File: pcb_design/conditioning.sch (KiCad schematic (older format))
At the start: 39 parts, among them U3 OPA2376AID, U4 LM2903-SO8

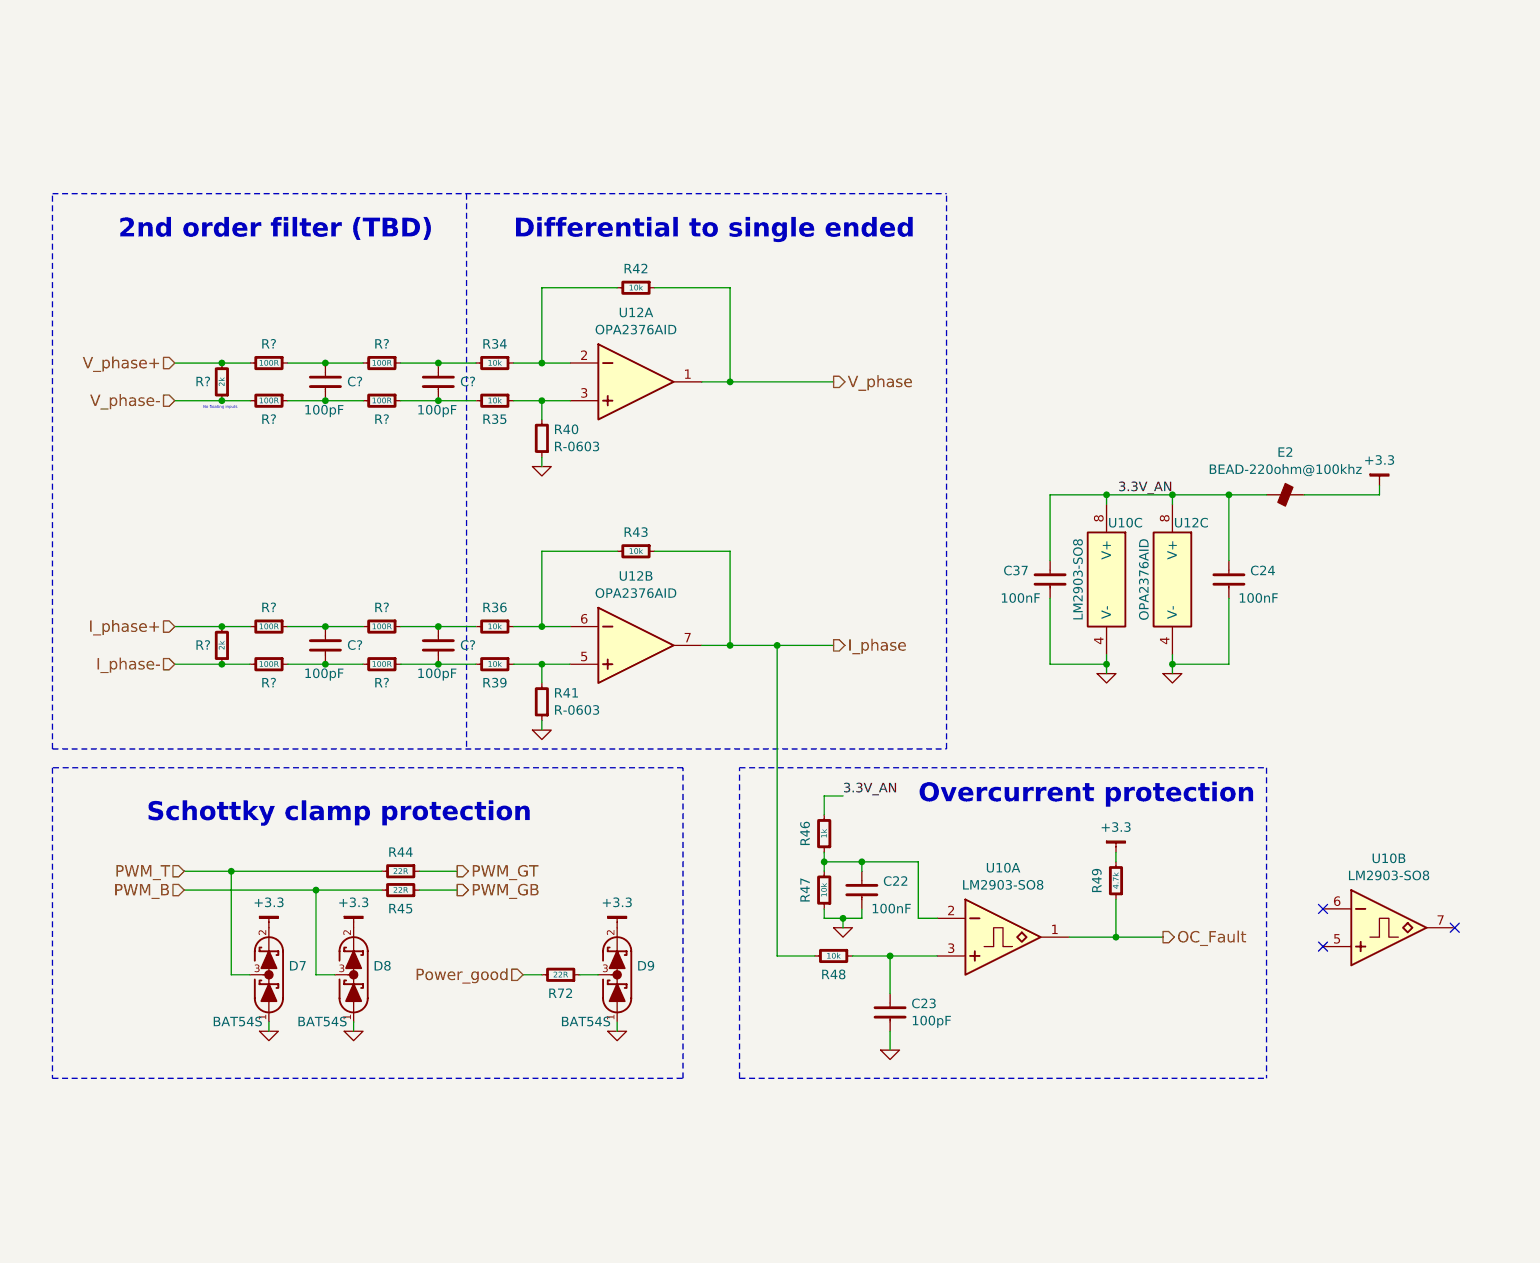
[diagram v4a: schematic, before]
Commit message: Added bus voltage conditioning, %v to accel and regen inputs, regulator diode, annotated schematic
Signed-off-by: Marcos Chaparro <mchaparro@paltatech.com>
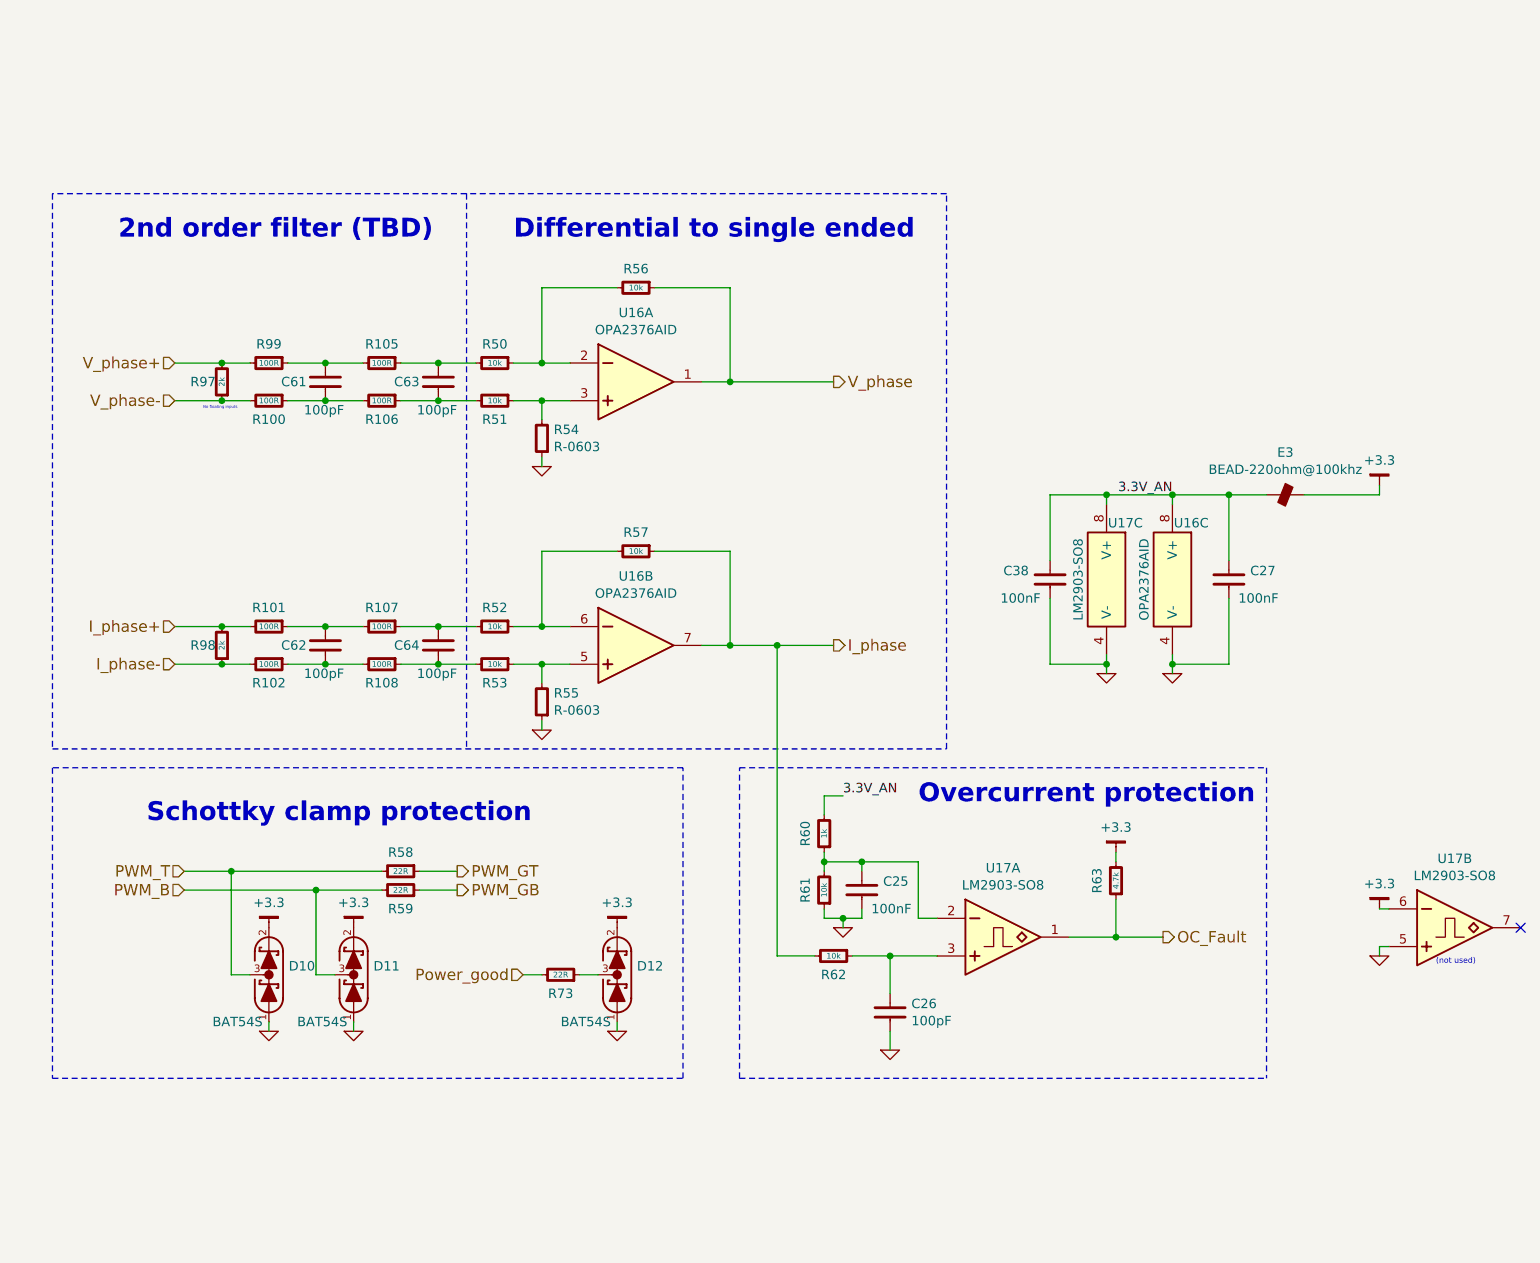
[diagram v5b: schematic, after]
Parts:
- gave numbers to parts that had none: 14
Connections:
- net +3.3: now also U4.6 (IN-)
- net GND: now also U4.5 (IN+)
- no-connect marks 3 -> 1
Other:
- note added: "(not used)"
- moved on the sheet: U17B

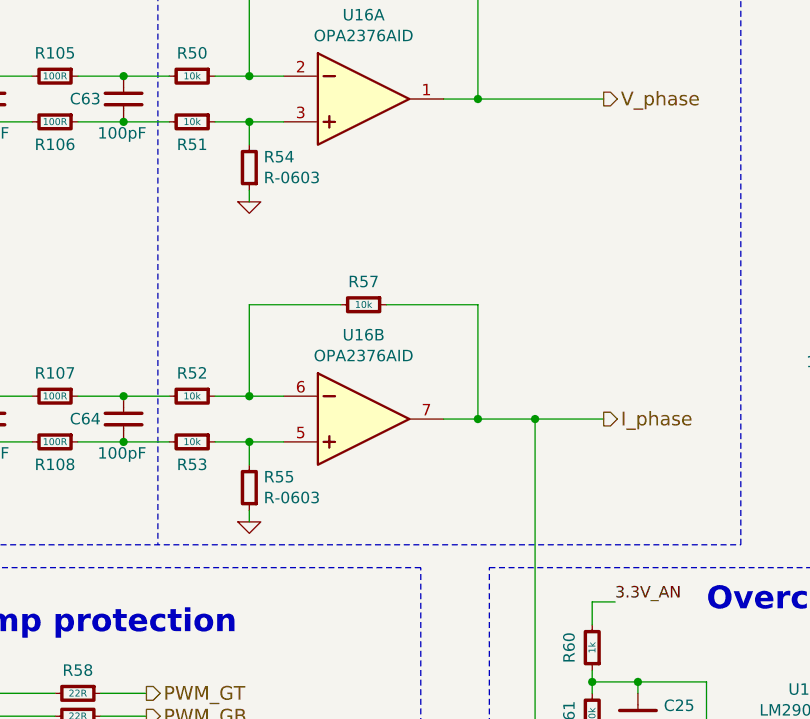
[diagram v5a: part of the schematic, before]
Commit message: Fixed issue with non-bidirectional phase current measurement. Started routing power supplies. Changed terminal blocks from 5.00mm to 3.81mm pitch
Signed-off-by: Marcos Chaparro <mchaparro@paltatech.com>
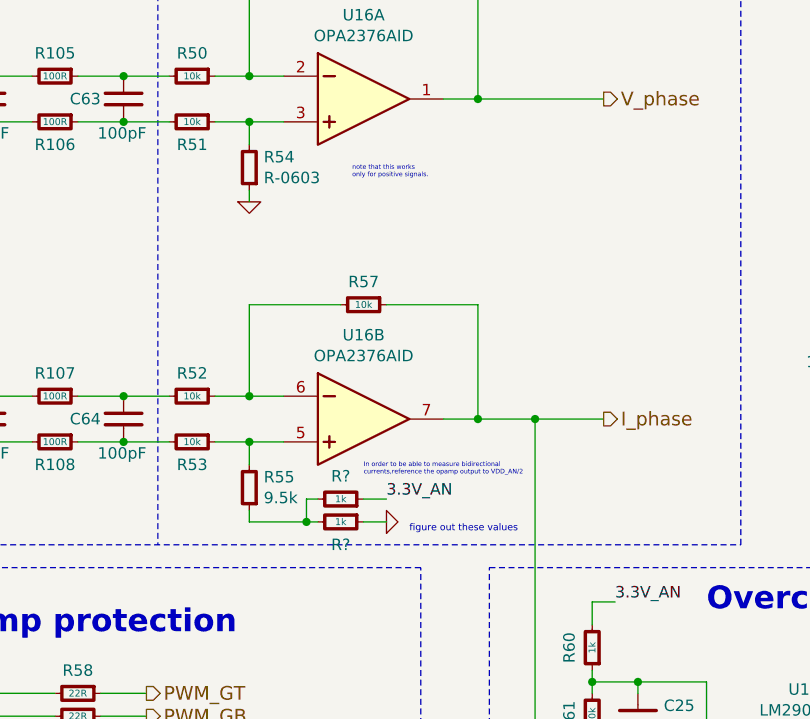
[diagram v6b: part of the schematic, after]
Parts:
- added R? (x2): 1k, IPC7351-Nominal:RESC1608X50, symbol R-0603
- R17: value R-0603 -> 9.5k
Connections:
- net 3.3V_AN: now also R?.1
- net GND: now also R?.1; no longer R17.1
- new net: R17.1, R?.2, R?.2
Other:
- note added: "In order to be able to measure bidirectional\ncurrents,reference the opamp output to VDD_AN/2"
- note added: "figure out these values"
- note added: "note that this works\nonly for positive signals."

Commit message: More layout
Signed-off-by: Marcos Chaparro <mchaparro@paltatech.com>
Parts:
- gave numbers to parts that had none: 2
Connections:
- net V_diff_+: now reaches C55.1, R4.2, R82.1
- net V_diff_-: now reaches C55.2, R5.2, R83.1
- net I_diff_+: now reaches C56.1, R14.2, R84.1
- net I_diff_-: now reaches C56.2, R15.2, R85.1
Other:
- note added: "For single-ended signals you can\nshort FB resistor, remove R_- and\ndrive your signal through IN+ of\nthe opamp so its a voltage follower"
- note added: "R_-"
- note added: "R_FB"
- note added: "figure out these values\ndo I need a C?"
- note removed: "figure out these values"
